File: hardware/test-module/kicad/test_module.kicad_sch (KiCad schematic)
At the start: 15 parts, among them J1 Barrel_Jack_12V, M1 ERM_Motor, M2 Stepper_4wire, M3 Servo_3pin, U1 D24V22F5_Buck, U2 Pi_Pico_W, U3 DRV2605L_Breakout, U4 DRV8871_Breakout, U5 Tic_T500, U6 Waveshare_2CH_RS232

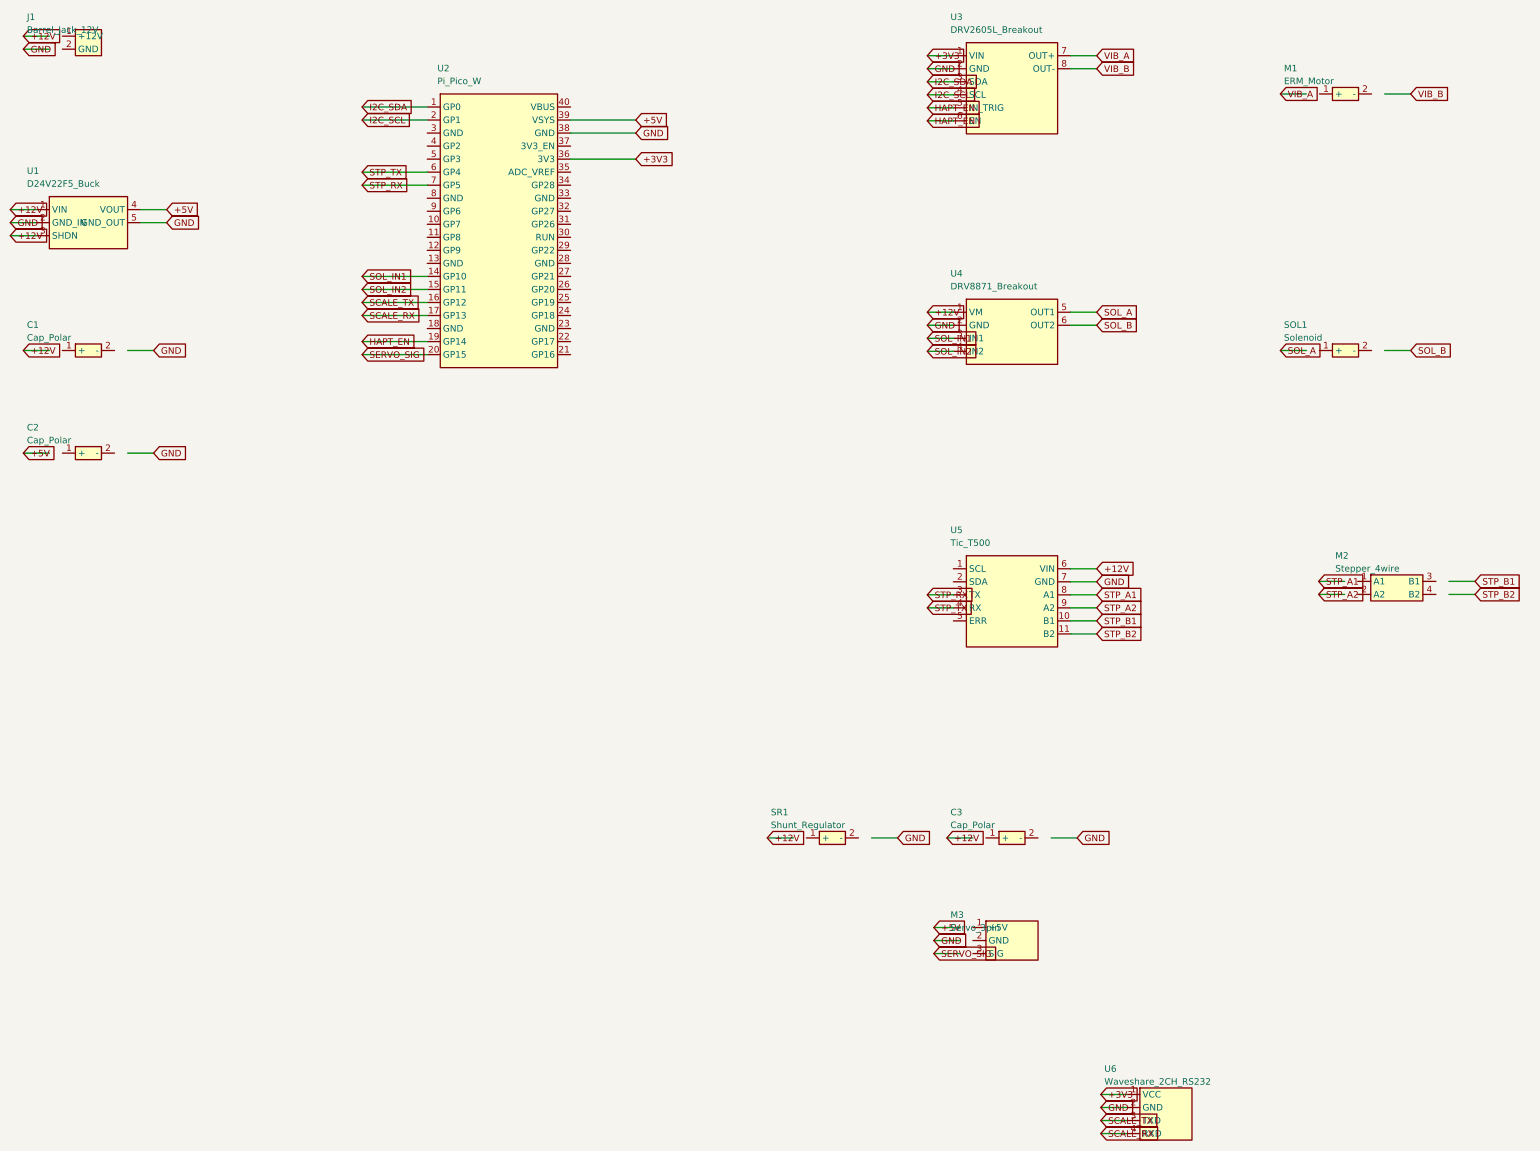
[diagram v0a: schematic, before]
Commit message: Drive the dispensing angle with two servos in unison (M3 GP15 + M4 GP2)
The bench now runs two HD-1810MG servos on opposite sides of the
baseplate (per PR #61); every angle command reaches both PWMs, with
servo 2 mirrored about the range midpoint when SERVO2_INVERT is set.

- config.py: PIN_SERVO_SIG2 = 2, SERVO2_INVERT = True
- main.py: dual-servo Servo class (pwm1/pwm2, _mirror), state() shows
  both pins + invert flag
- tests/test_servo.py: drives both servos; 'i' toggles mirroring live
- KiCad: M4 servo on SERVO_SIG2/GP2, rev C; fixed SYMBOL_PINS offsets
  that left every actuator symbol (J1, C1-C3, M1-M4, SOL1, SR1)
  electrically unconnected in the exported netlist (labels sat 2.54 mm
  off the pin anchors); netlist now verifies GP15<->M3.SIG,
  GP2<->M4.SIG and full power-rail membership; renders regenerated
- sim tests: DualServoTests (mirrored + non-inverted paths); fixed the
  stale parity assertion that broke when config.py moved to the bench
  balance's 19200 8N1 preset; suite 30/30

Co-authored-by: William Mulberry <98996414+williamulbz@users.noreply.github.com>
Co-Authored-By: Claude Fable 5 <noreply@anthropic.com>
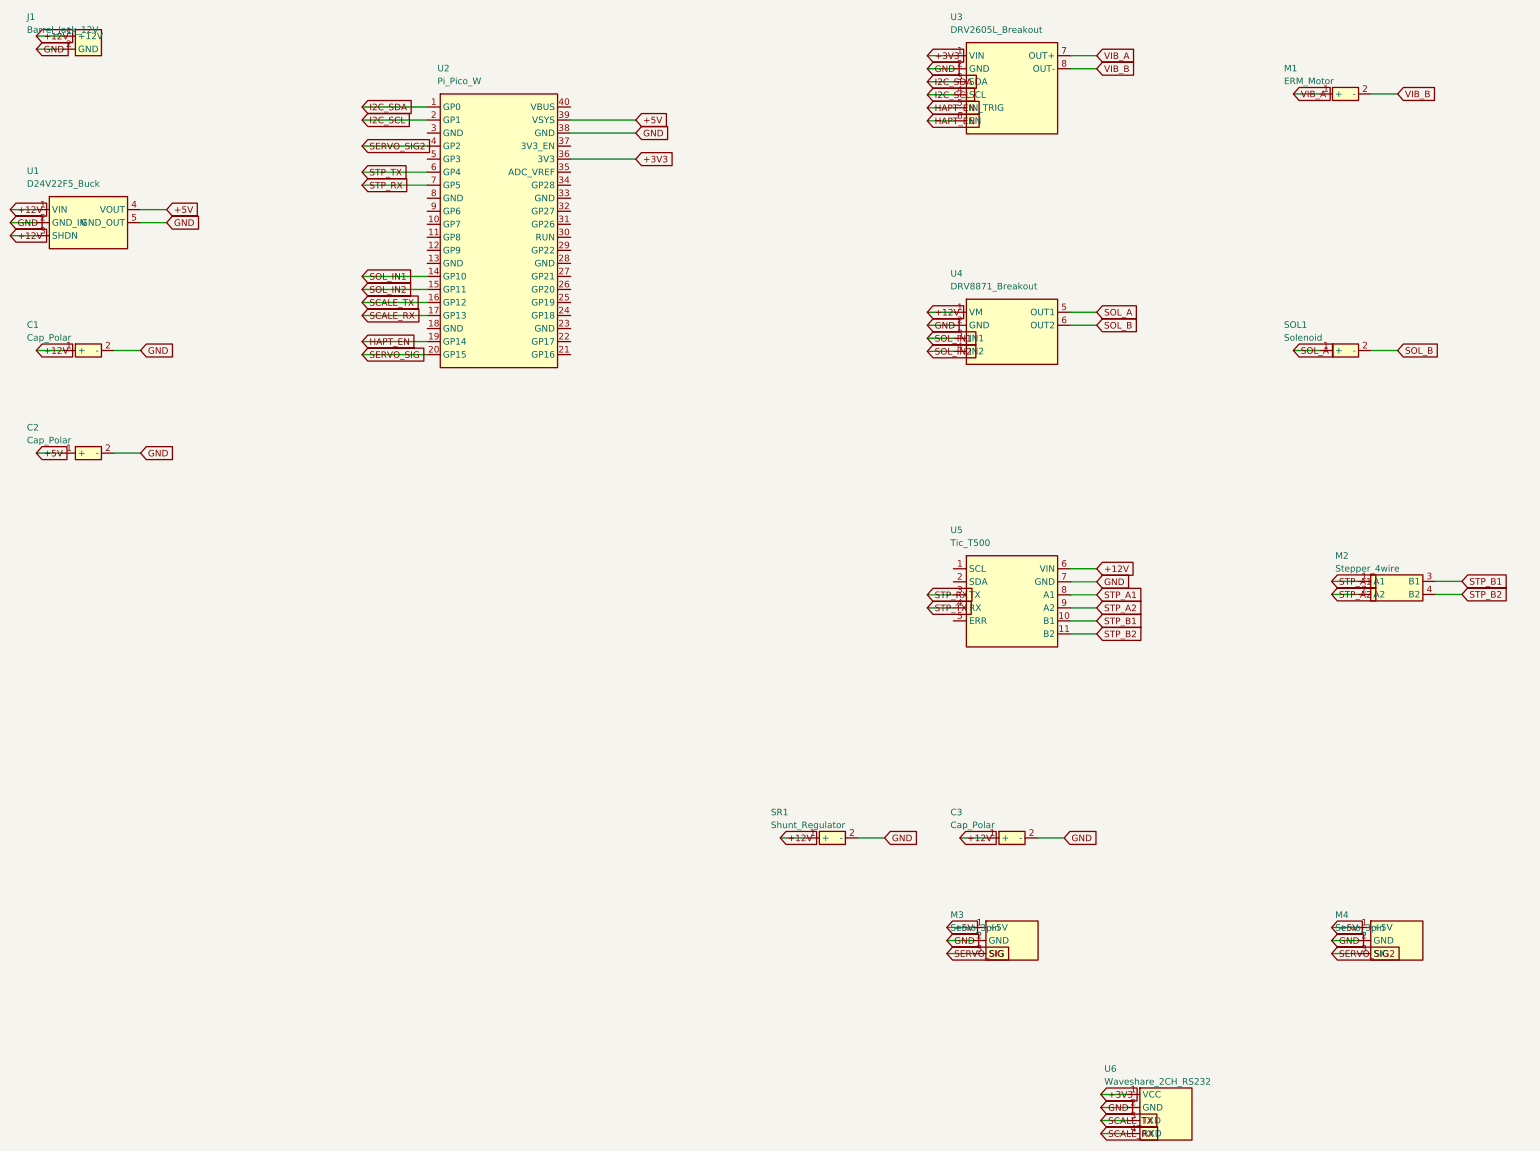
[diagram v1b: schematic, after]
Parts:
- added M4: Servo_3pin, symbol test_module:Servo_3pin
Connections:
- net +12V: now also C1.1 (+), C3.1 (+), J1.1 (+12V), SR1.1 (+)
- net +5V: now also C2.1 (+), M3.1 (+5V), M4.1 (+5V)
- net GND: now also C1.2 (-), C2.2 (-), C3.2 (-), J1.2 (GND), M3.2 (GND), SR1.2 (-), M4.2 (GND)
- net SERVO_SIG: now also M3.3 (SIG)
- net SOL_A: now also SOL1.1 (+)
- net SOL_B: now also SOL1.2 (-)
- net STP_A1: now also M2.1 (A1)
- net STP_A2: now also M2.2 (A2)
- net STP_B1: now also M2.3 (B1)
- net STP_B2: now also M2.4 (B2)
- net VIB_A: now also M1.1 (+)
- net VIB_B: now also M1.2 (-)
- net SERVO_SIG2: now reaches U2.4 (GP2)
- net SERVO_SIG2: now also M4.3 (SIG)
